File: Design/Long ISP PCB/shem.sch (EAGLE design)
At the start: 33 parts, among them IC1 4511N, IC2 4511N, J1 9V_POWER_JACK, Q1 600mA/40V, Q2 600mA/40V, Q3 600mA/40V, Q4 600mA/40V, Q5 600mA/40V, U2 328P, U3 SN74HC595N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

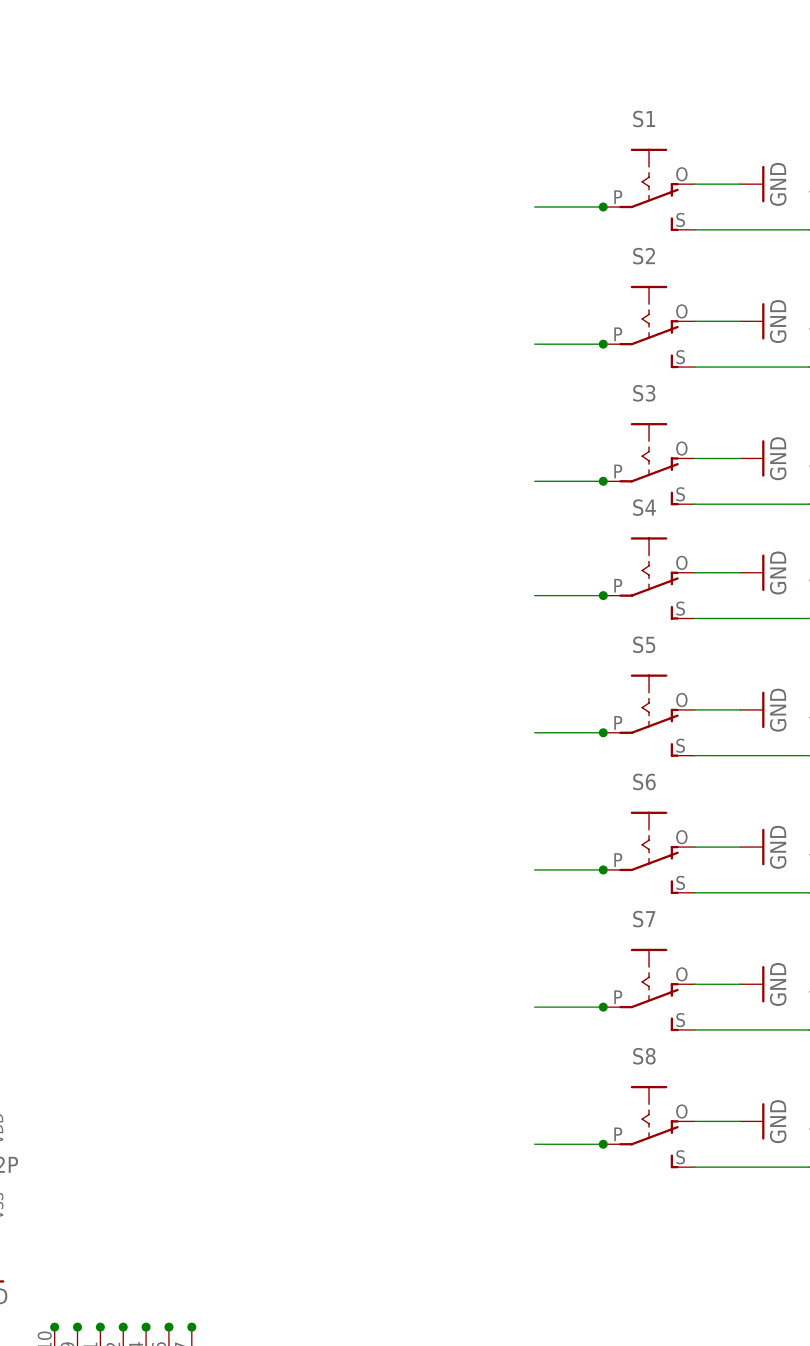
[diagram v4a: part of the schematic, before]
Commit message: re added led indicators to inputswitches
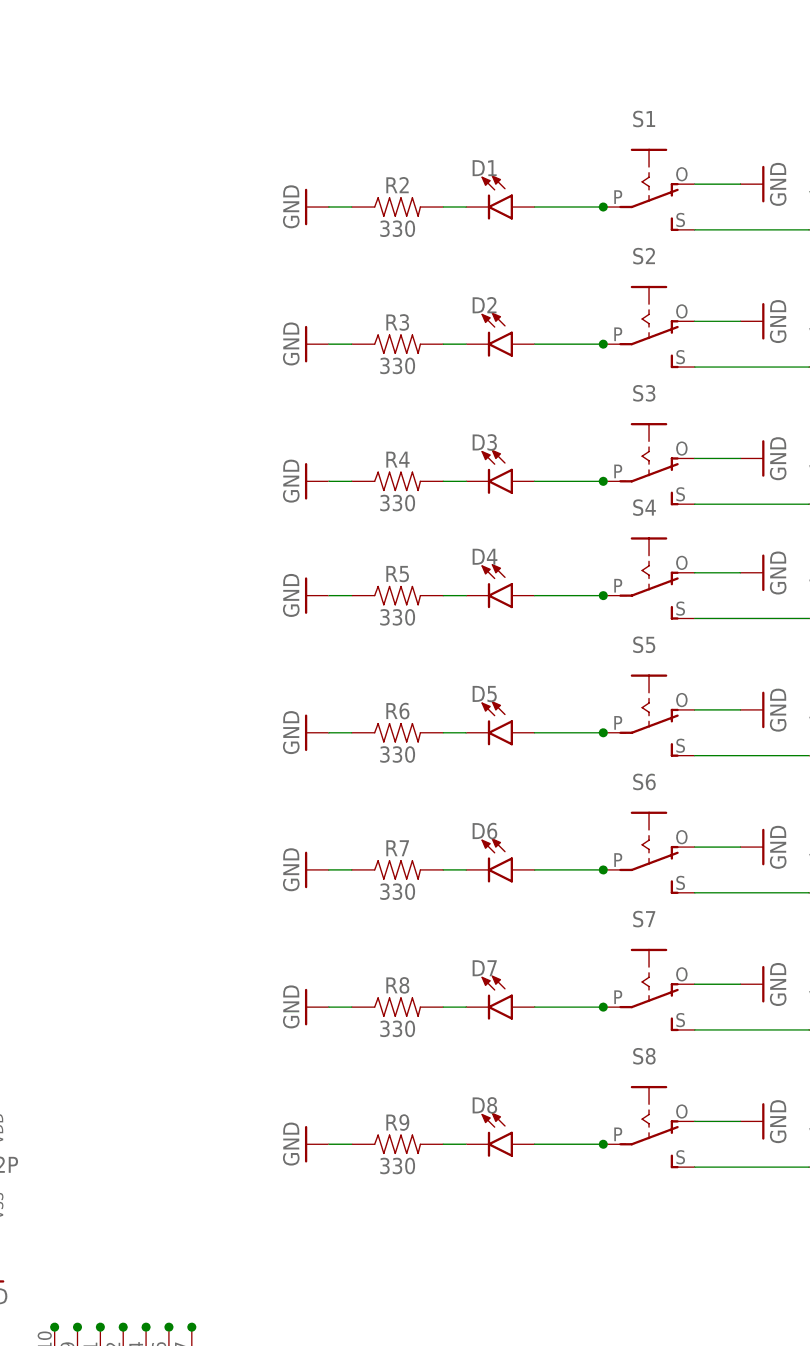
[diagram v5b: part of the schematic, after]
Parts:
- added D1, D2, D3, D4, D5, D6, D7, D8: (no value), SparkFun-LED:LED3MM
- added R2, R3, R4, R5, R6, R7, R8, R9: 330, SparkFun-Resistors:330OHM-HORIZ-1/10W-5%
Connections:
- new net N$12: D1.C, R2.2
- new net N$13: D8.C, R9.2
- new net N$14: D7.C, R8.2
- new net N$15: D6.C, R7.2
- new net N$17: D5.C, R6.2
- new net N$18: D4.C, R5.2
- new net N$19: D3.C, R4.2
- new net N$20: D2.C, R3.2
- net GND: now also R2.1, R3.1, R4.1, R5.1, R6.1, R7.1, R8.1, R9.1
- net S0: now also D1.A
- net S1: now also D2.A
- net S2: now also D3.A
- net S3: now also D4.A
- net S4: now also D5.A
- net S5: now also D6.A
- net S6: now also D7.A
- net S7: now also D8.A
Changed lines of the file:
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@@
 <part name="PWR" library="adafruit" deviceset="EG1218" device="S"/>
 <part name="P+1" library="supply1" deviceset="VCC" device=""/>
+<part name="R2" library="SparkFun-Resistors" deviceset="330OHM" device="-HORIZ-1/10W-5%" value="330"/>
+<part name="D1" library="SparkFun-LED" deviceset="LED" device="3MM"/>
+<part name="GND25" library="supply1" deviceset="GND" device=""/>
+<part name="R3" library="SparkFun-Resistors" deviceset="330OHM" device="-HORIZ-1/10W-5%" value="330"/>
+<part name="D2" library="SparkFun-LED" deviceset="LED" device="3MM"/>
+<part name="GND26" library="supply1" deviceset="GND" device=""/>
+<part name="GND27" library="supply1" deviceset="GND" device=""/>
+<part name="R4" library="SparkFun-Resistors" deviceset="330OHM" device="-HORIZ-1/10W-5%" value="330"/>
+<part name="D3" library="SparkFun-LED" deviceset="LED" device="3MM"/>
+<part name="D4" library="SparkFun-LED" deviceset="LED" device="3MM"/>
+<part name="D5" library="SparkFun-LED" deviceset="LED" device="3MM"/>
+<part name="D6" library="SparkFun-LED" deviceset="LED" device="3MM"/>
+<part name="D7" library="SparkFun-LED" deviceset="LED" device="3MM"/>
+<part name="D8" library="SparkFun-LED" deviceset="LED" device="3MM"/>
+<part name="R5" library="SparkFun-Resistors" deviceset="330OHM" device="-HORIZ-1/10W-5%" value="330"/>
+<part name="R6" library="SparkFun-Resistors" deviceset="330OHM" device="-HORIZ-1/10W-5%" value="330"/>
+<part name="R7" library="SparkFun-Resistors" deviceset="330OHM" device="-HORIZ-1/10W-5%" value="330"/>
+<part name="R8" library="SparkFun-Resistors" deviceset="330OHM" device="-HORIZ-1/10W-5%" value="330"/>
+<part name="R9" library="SparkFun-Resistors" deviceset="330OHM" device="-HORIZ-1/10W-5%" value="330"/>
+<part name="GND28" library="supply1" deviceset="GND" device=""/>
+<part name="GND29" library="supply1" deviceset="GND" device=""/>
+<part name="GND30" library="supply1" deviceset="GND" device=""/>
+<part name="GND31" library="supply1" deviceset="GND" device=""/>
+<part name="GND32" library="supply1" deviceset="GND" device=""/>
 </parts>
 <sheets>
@@
 <instance part="PWR" gate="1" x="33.02" y="114.3" rot="R180"/>
 <instance part="P+1" gate="VCC" x="30.48" y="124.46"/>
+<instance part="R2" gate="G$1" x="182.88" y="149.86"/>
+<instance part="D1" gate="G$1" x="195.58" y="149.86" rot="R270"/>
+<instance part="GND25" gate="1" x="172.72" y="149.86" rot="R270"/>
+<instance part="R3" gate="G$1" x="182.88" y="134.62"/>
+<instance part="D2" gate="G$1" x="195.58" y="134.62" rot="R270"/>
+<instance part="GND26" gate="1" x="172.72" y="134.62" rot="R270"/>
+<instance part="GND27" gate="1" x="172.72" y="119.38" rot="R270"/>
+<instance part="R4" gate="G$1" x="182.88" y="119.38"/>
+<instance part="D3" gate="G$1" x="195.58" y="119.38" rot="R270"/>
+<instance part="D4" gate="G$1" x="195.58" y="106.68" rot="R270"/>
+<instance part="D5" gate="G$1" x="195.58" y="91.44" rot="R270"/>
+<instance part="D6" gate="G$1" x="195.58" y="76.2" rot="R270"/>
+<instance part="D7" gate="G$1" x="195.58" y="60.96" rot="R270"/>
+<instance part="D8" gate="G$1" x="195.58" y="45.72" rot="R270"/>
+<instance part="R5" gate="G$1" x="182.88" y="106.68"/>
+<instance part="R6" gate="G$1" x="182.88" y="91.44"/>
+<instance part="R7" gate="G$1" x="182.88" y="76.2"/>
+<instance part="R8" gate="G$1" x="182.88" y="60.96"/>
+<instance part="R9" gate="G$1" x="182.88" y="45.72"/>
+<instance part="GND28" gate="1" x="172.72" y="106.68" rot="R270"/>
+<instance part="GND29" gate="1" x="172.72" y="91.44" rot="R270"/>
+<instance part="GND30" gate="1" x="172.72" y="76.2" rot="R270"/>
+<instance part="GND31" gate="1" x="172.72" y="60.96" rot="R270"/>
+<instance part="GND32" gate="1" x="172.72" y="45.72" rot="R270"/>
 </instances>
 <busses>
@@
 <wire x1="50.8" y1="-20.32" x2="50.8" y2="-17.78" width="0.1524" layer="91"/>
 </segment>
+<segment>
+<pinref part="R2" gate="G$1" pin="1"/>
+<pinref part="GND25" gate="1" pin="GND"/>
+<wire x1="175.26" y1="149.86" x2="177.8" y2="149.86" width="0.1524" layer="91"/>
+</segment>
+<segment>
+<pinref part="GND26" gate="1" pin="GND"/>
+<pinref part="R3" gate="G$1" pin="1"/>
+<wire x1="175.26" y1="134.62" x2="177.8" y2="134.62" width="0.1524" layer="91"/>
+</segment>
+<segment>
+<pinref part="GND27" gate="1" pin="GND"/>
+<pinref part="R4" gate="G$1" pin="1"/>
+<wire x1="175.26" y1="119.38" x2="177.8" y2="119.38" width="0.1524" layer="91"/>
+</segment>
+<segment>
+<pinref part="GND28" gate="1" pin="GND"/>
+<pinref part="R5" gate="G$1" pin="1"/>
+<wire x1="175.26" y1="106.68" x2="177.8" y2="106.68" width="0.1524" layer="91"/>
+</segment>
+<segment>
+<pinref part="GND29" gate="1" pin="GND"/>
+<pinref part="R6" gate="G$1" pin="1"/>
+<wire x1="175.26" y1="91.44" x2="177.8" y2="91.44" width="0.1524" layer="91"/>
+</segment>
+<segment>
+<pinref part="GND30" gate="1" pin="GND"/>
+<pinref part="R7" gate="G$1" pin="1"/>
+<wire x1="175.26" y1="76.2" x2="177.8" y2="76.2" width="0.1524" layer="91"/>
+</segment>
+<segment>
+<pinref part="GND31" gate="1" pin="GND"/>
+<pinref part="R8" gate="G$1" pin="1"/>
+<wire x1="175.26" y1="60.96" x2="177.8" y2="60.96" width="0.1524" layer="91"/>
+</segment>
+<segment>
+<pinref part="GND32" gate="1" pin="GND"/>
+<pinref part="R9" gate="G$1" pin="1"/>
+<wire x1="175.26" y1="45.72" x2="177.8" y2="45.72" width="0.1524" layer="91"/>
+</segment>
 </net>
 <net name="SCK" class="0">
@@
 <junction x="205.74" y="149.86"/>
 <wire x1="198.12" y1="149.86" x2="205.74" y2="149.86" width="0.1524" layer="91"/>
+<pinref part="D1" gate="G$1" pin="A"/>
 </segment>
 </net>
@@
 <junction x="205.74" y="134.62"/>
 <wire x1="198.12" y1="134.62" x2="205.74" y2="134.62" width="0.1524" layer="91"/>
+<pinref part="D2" gate="G$1" pin="A"/>
 </segment>
 </net>
@@
 <junction x="205.74" y="119.38"/>
 <wire x1="198.12" y1="119.38" x2="205.74" y2="119.38" width="0.1524" layer="91"/>
+<pinref part="D3" gate="G$1" pin="A"/>
 </segment>
 </net>
@@
 <junction x="205.74" y="106.68"/>
 <wire x1="198.12" y1="106.68" x2="205.74" y2="106.68" width="0.1524" layer="91"/>
+<pinref part="D4" gate="G$1" pin="A"/>
 </segment>
 </net>
@@
 <junction x="205.74" y="91.44"/>
 <wire x1="198.12" y1="91.44" x2="205.74" y2="91.44" width="0.1524" layer="91"/>
+<pinref part="D5" gate="G$1" pin="A"/>
 </segment>
 </net>
@@
 <junction x="205.74" y="60.96"/>
 <wire x1="198.12" y1="60.96" x2="205.74" y2="60.96" width="0.1524" layer="91"/>
+<pinref part="D7" gate="G$1" pin="A"/>
 </segment>
 </net>
@@
 <junction x="205.74" y="76.2"/>
 <wire x1="198.12" y1="76.2" x2="205.74" y2="76.2" width="0.1524" layer="91"/>
+<pinref part="D6" gate="G$1" pin="A"/>
 </segment>
 </net>
@@
 <junction x="205.74" y="45.72"/>
 <wire x1="198.12" y1="45.72" x2="205.74" y2="45.72" width="0.1524" layer="91"/>
+<pinref part="D8" gate="G$1" pin="A"/>
 </segment>
 </net>
@@
 </segment>
 </net>
+<net name="N$12" class="0">
+<segment>
+<pinref part="D1" gate="G$1" pin="C"/>
+<pinref part="R2" gate="G$1" pin="2"/>
+<wire x1="187.96" y1="149.86" x2="190.5" y2="149.86" width="0.1524" layer="91"/>
+</segment>
+</net>
+<net name="N$13" class="0">
+<segment>
+<pinref part="R9" gate="G$1" pin="2"/>
+<pinref part="D8" gate="G$1" pin="C"/>
+<wire x1="187.96" y1="45.72" x2="190.5" y2="45.72" width="0.1524" layer="91"/>
+</segment>
+</net>
+<net name="N$14" class="0">
+<segment>
+<pinref part="R8" gate="G$1" pin="2"/>
+<pinref part="D7" gate="G$1" pin="C"/>
+<wire x1="187.96" y1="60.96" x2="190.5" y2="60.96" width="0.1524" layer="91"/>
+</segment>
+</net>
+<net name="N$15" class="0">
+<segment>
+<pinref part="R7" gate="G$1" pin="2"/>
+<pinref part="D6" gate="G$1" pin="C"/>
+<wire x1="187.96" y1="76.2" x2="190.5" y2="76.2" width="0.1524" layer="91"/>
+</segment>
+</net>
+<net name="N$17" class="0">
+<segment>
+<pinref part="R6" gate="G$1" pin="2"/>
+<pinref part="D5" gate="G$1" pin="C"/>
+<wire x1="187.96" y1="91.44" x2="190.5" y2="91.44" width="0.1524" layer="91"/>
+</segment>
+</net>
+<net name="N$18" class="0">
+<segment>
+<pinref part="D4" gate="G$1" pin="C"/>
+<pinref part="R5" gate="G$1" pin="2"/>
+<wire x1="190.5" y1="106.68" x2="187.96" y2="106.68" width="0.1524" layer="91"/>
+</segment>
+</net>
+<net name="N$19" class="0">
+<segment>
+<pinref part="R4" gate="G$1" pin="2"/>
+<pinref part="D3" gate="G$1" pin="C"/>
+<wire x1="187.96" y1="119.38" x2="190.5" y2="119.38" width="0.1524" layer="91"/>
+</segment>
+</net>
+<net name="N$20" class="0">
+<segment>
+<pinref part="R3" gate="G$1" pin="2"/>
+<pinref part="D2" gate="G$1" pin="C"/>
+<wire x1="187.96" y1="134.62" x2="190.5" y2="134.62" width="0.1524" layer="91"/>
+</segment>
+</net>
